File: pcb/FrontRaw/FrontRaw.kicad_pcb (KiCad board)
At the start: 2 copper layers, 54.5 x 106.4 mm, 13 parts

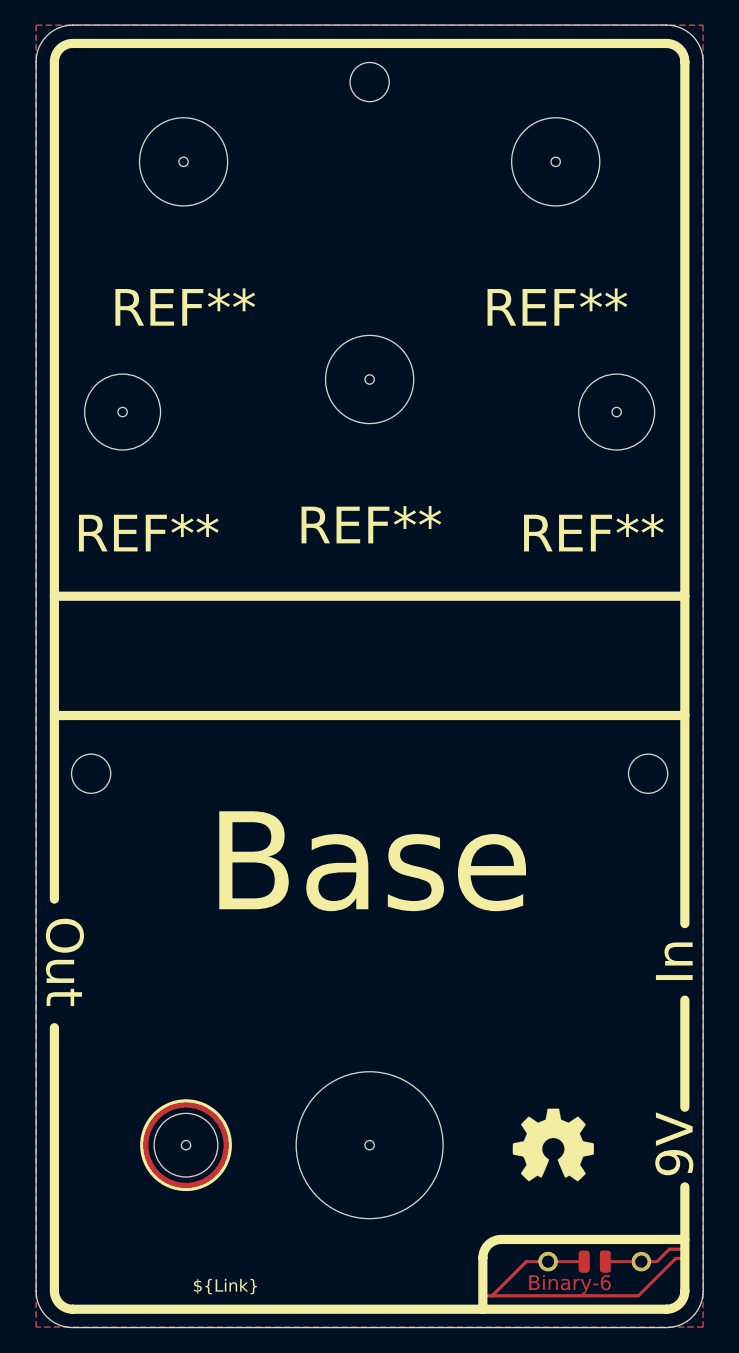
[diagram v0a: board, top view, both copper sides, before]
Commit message: [AllRaw] Update base templates to 6 controls design
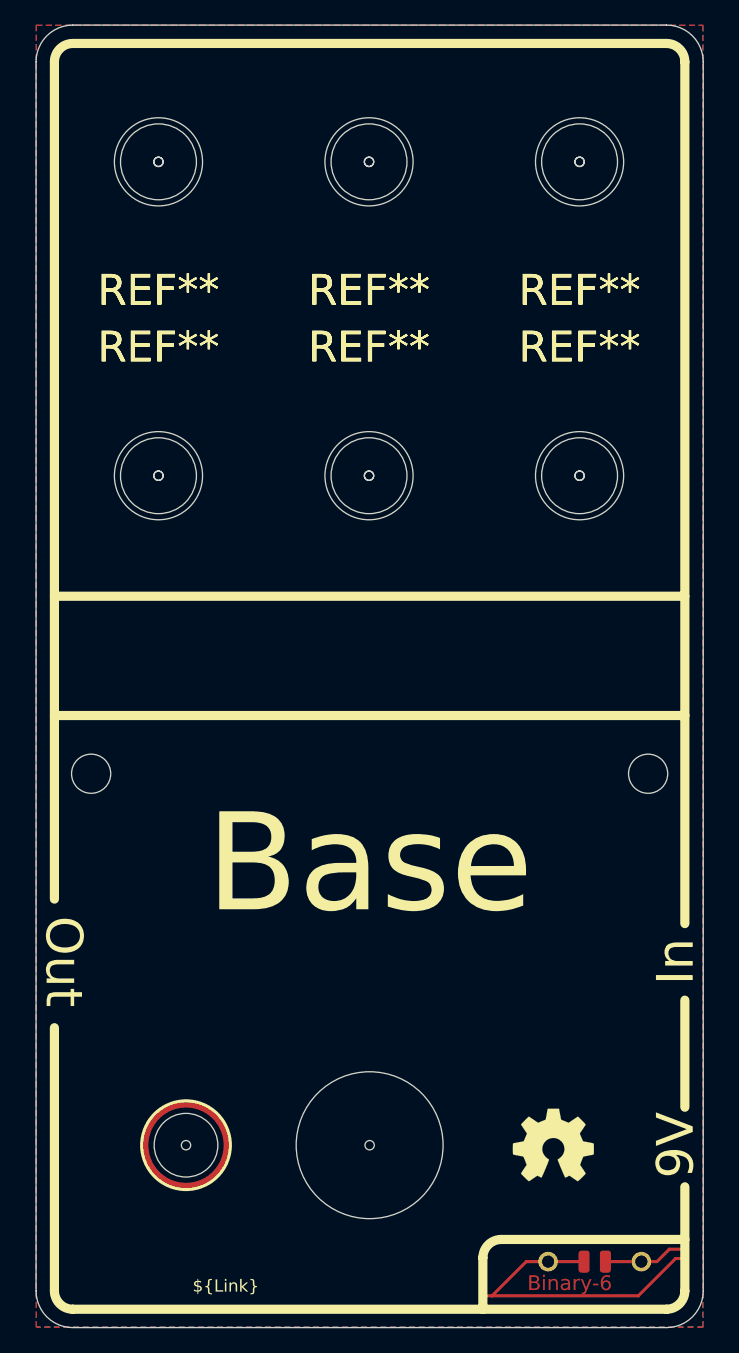
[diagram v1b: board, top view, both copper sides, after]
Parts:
- removed the MK2 at (149.5, 63.1)
- added REF**: Drill_ToggleSwitch_6,2mm, MeineBib:Drill_ToggleSwitch_6,2mm, F.Cu at (149.4, 95.3)
- added REF**: Drill_ToggleSwitch_6,2mm, MeineBib:Drill_ToggleSwitch_6,2mm, F.Cu at (166.7, 69.6)
- added REF**: Drill_9mmPot_7,2mm, MeineBib:Drill_9mmPot_7,2mm, F.Cu at (132.2, 95.3)
- added REF**: Drill_ToggleSwitch_6,2mm, MeineBib:Drill_ToggleSwitch_6,2mm, F.Cu at (166.7, 95.3)
- added REF**: Drill_9mmPot_7,2mm, MeineBib:Drill_9mmPot_7,2mm, F.Cu at (149.4, 95.3)
- added REF**: Drill_9mmPot_7,2mm, MeineBib:Drill_9mmPot_7,2mm, F.Cu at (166.7, 95.3)
- added REF**: Drill_ToggleSwitch_6,2mm, MeineBib:Drill_ToggleSwitch_6,2mm, F.Cu at (149.4, 69.6)
- moved REF** 37.8 mm to (132.2, 95.3), turned to 180 degrees
- moved REF** 24.7 mm to (166.7, 69.6)
- moved REF** 20.6 mm to (132.2, 69.6)
- moved REF** 15.2 mm to (149.4, 69.6)
- moved MK6 8.86 mm to (149.5, 81.6)
- moved REF** 2.05 mm to (132.2, 69.6)
